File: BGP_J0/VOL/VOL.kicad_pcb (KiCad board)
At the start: 2 copper layers, 28 x 25 mm, 28 parts, among them J1 Conn_01x03_Female, P1 CONN_01X03, P2 CONN_01X02, P3 CONN_01X04, P4 CONN_01X02, P5 CONN_01X03, Q1 MMBF5457, Q2 MMBF5457

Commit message: Revert some changes
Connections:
- RV2 pad 1: /OUT -> Net-(RV2-Pad1)
- RV2 pad 3: Net-(RV2-Pad3) -> /I_BY
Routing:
- net /OUT: track 35.1 -> 28.5 mm
- net /I_BY: track 19.9 -> 24.2 mm

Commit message: Final J0 tone pot fixes
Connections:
- RV2 pad 1: Net-(RV2-Pad1) -> Net-(J1-Pad1)
- RV2 pad 2: Net-(J1-Pad1) -> /I_BY
- RV2 pad 3: /I_BY -> Net-(RV2-Pad3)
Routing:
- net Net-(J1-Pad1): track 10.4 -> 7.29 mm
- net /I_BY: track 24.2 -> 26.9 mm
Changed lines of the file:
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@@
   (general
     (links 49)
-    (no_connects 0)
+    (no_connects 3)
     (area 150.924999 70.924999 179.075001 96.075001)
     (thickness 1.6)
     (drawings 8)
-    (tracks 146)
+    (tracks 147)
     (zones 0)
     (modules 28)
@@
   (net 16 "Net-(J1-Pad2)")
   (net 17 "Net-(J1-Pad1)")
-  (net 18 "Net-(RV2-Pad1)")
+  (net 18 "Net-(RV2-Pad3)")
   (net_class Default "This is the default net class."
     (clearance 0.3)
@@
     (add_net "Net-(P1-Pad3)")
     (add_net "Net-(Q1-Pad2)")
-    (add_net "Net-(RV2-Pad1)")
+    (add_net "Net-(RV2-Pad3)")
   )
   (net_class PWR ""
@@
     (fp_line (start 2.1 10.7) (end -12.15 10.7) (layer B.CrtYd) (width 0.05))
     (pad 3 thru_hole circle (at 0 7.5 180) (size 1.8 1.8) (drill 1) (layers *.Cu *.Mask)
+      (net 18 "Net-(RV2-Pad3)"))
+    (pad 2 thru_hole circle (at 0 3.75 180) (size 1.8 1.8) (drill 1) (layers *.Cu *.Mask)
       (net 13 /I_BY))
-    (pad 2 thru_hole circle (at 0 3.75 180) (size 1.8 1.8) (drill 1) (layers *.Cu *.Mask)
+    (pad 1 thru_hole circle (at 0 0 180) (size 1.8 1.8) (drill 1) (layers *.Cu *.Mask)
       (net 17 "Net-(J1-Pad1)"))
-    (pad 1 thru_hole circle (at 0 0 180) (size 1.8 1.8) (drill 1) (layers *.Cu *.Mask)
-      (net 18 "Net-(RV2-Pad1)"))
     (pad 6 thru_hole circle (at -5 7.5 180) (size 1.8 1.8) (drill 1) (layers *.Cu *.Mask)
       (net 13 /I_BY))
@@
   (segment (start 162.8 88.1) (end 162.8 87.95) (width 0.3) (layer F.Cu) (net 12))
   (segment (start 163.8 73.3) (end 163.8 73.55) (width 0.3) (layer B.Cu) (net 12))
-  (segment (start 155.2 79.8) (end 155.25 79.85) (width 0.5) (layer F.Cu) (net 13))
-  (segment (start 155.2 73.3) (end 155.2 79.8) (width 0.5) (layer F.Cu) (net 13))
-  (segment (start 158 79.85) (end 155.25 79.85) (width 0.5) (layer F.Cu) (net 13))
+  (segment (start 158 79.85) (end 154.25 83.6) (width 0.5) (layer F.Cu) (net 13))
+  (segment (start 154.25 83.6) (end 153 83.6) (width 0.5) (layer F.Cu) (net 13))
+  (segment (start 155.2 73.3) (end 155.2 77.05) (width 0.5) (layer F.Cu) (net 13))
+  (segment (start 155.2 77.05) (end 158 79.85) (width 0.5) (layer F.Cu) (net 13))
   (segment (start 155.2 73.3) (end 155.2 73.05) (width 0.5) (layer F.Cu) (net 13))
   (segment (start 155.2 73.05) (end 156.5 71.75) (width 0.5) (layer F.Cu) (net 13))
@@
   (segment (start 165.8 73.05) (end 165.8 73.3) (width 0.5) (layer F.Cu) (net 13))
   (segment (start 164.5 71.75) (end 165.8 73.05) (width 0.5) (layer F.Cu) (net 13))
-  (segment (start 155.25 79.85) (end 153 79.85) (width 0.5) (layer F.Cu) (net 13))
   (segment (start 165.8 73.3) (end 165.8 73.05) (width 0.5) (layer B.Cu) (net 13))
   (segment (start 155.2 73.05) (end 155.2 73.3) (width 0.5) (layer B.Cu) (net 13))
@@
   (segment (start 174.4 92.7) (end 173.10051 92.7) (width 0.3) (layer F.Cu) (net 15))
   (segment (start 173.10051 92.7) (end 171 92.7) (width 0.5) (layer F.Cu) (net 15))
-  (segment (start 153 83.6) (end 155.46 86.06) (width 0.4) (layer F.Cu) (net 17))
-  (segment (start 155.46 86.06) (end 155.46 92.95) (width 0.4) (layer F.Cu) (net 17))
+  (segment (start 153 87.35) (end 153 91.64) (width 0.5) (layer F.Cu) (net 17))
+  (segment (start 153 91.64) (end 154.31 92.95) (width 0.5) (layer F.Cu) (net 17))
+  (segment (start 154.31 92.95) (end 155.46 92.95) (width 0.5) (layer F.Cu) (net 17))
   (zone (net 4) (net_name Earth) (layer B.Cu) (hatch edge 0.508)
     (connect_pads (clearance 0.3))

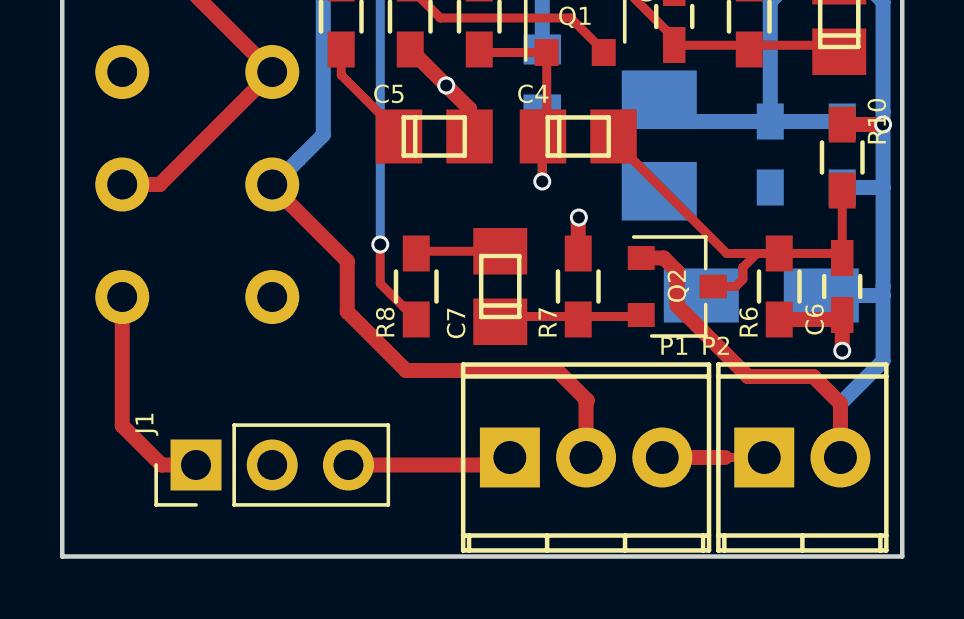
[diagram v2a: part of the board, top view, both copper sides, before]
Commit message: J0 VOL board modded for all CONN on bottom side
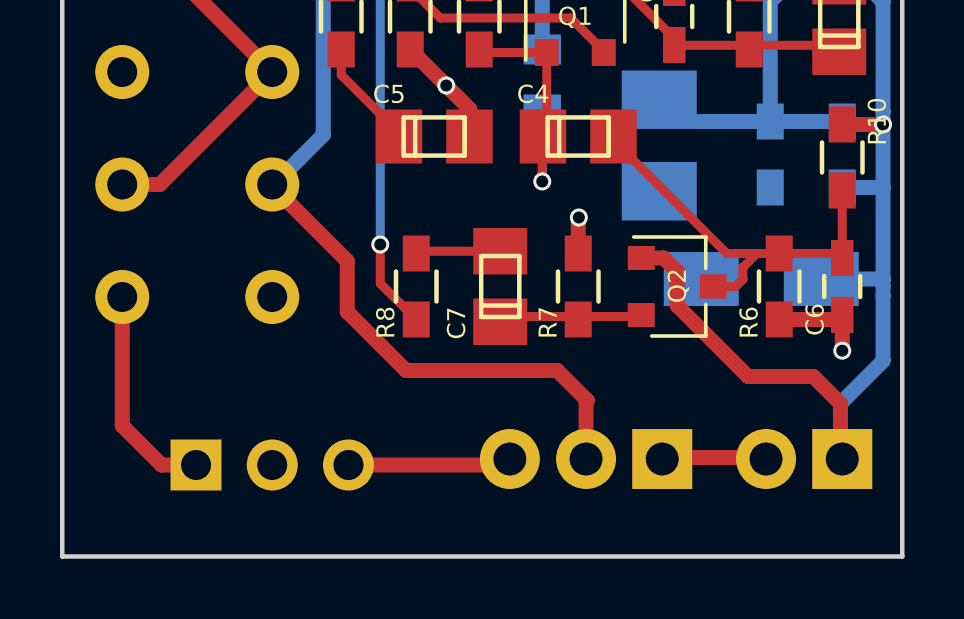
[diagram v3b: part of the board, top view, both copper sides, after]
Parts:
- J1, P1, P2: moved to B.Cu
- moved P1 5.08 mm to (171.0, 92.8), turned to 180 degrees
- moved P2 2.60 mm to (177.0, 92.8), turned to 180 degrees
- moved D1 0.55 mm to (174.3, 86.8)
- turned J1 to 270 degrees
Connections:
- P1 pad 1: Earth -> Net-(P1-Pad1)
- P1 pad 3: Net-(P1-Pad3) -> Earth
- P2 pad 1: Net-(P1-Pad3) -> VCC
- P2 pad 2: VCC -> Net-(P1-Pad1)
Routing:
- net Net-(P1-Pad3): track 3.40 -> 0.00 mm
- net Net-(P1-Pad1): track 0.00 -> 3.40 mm

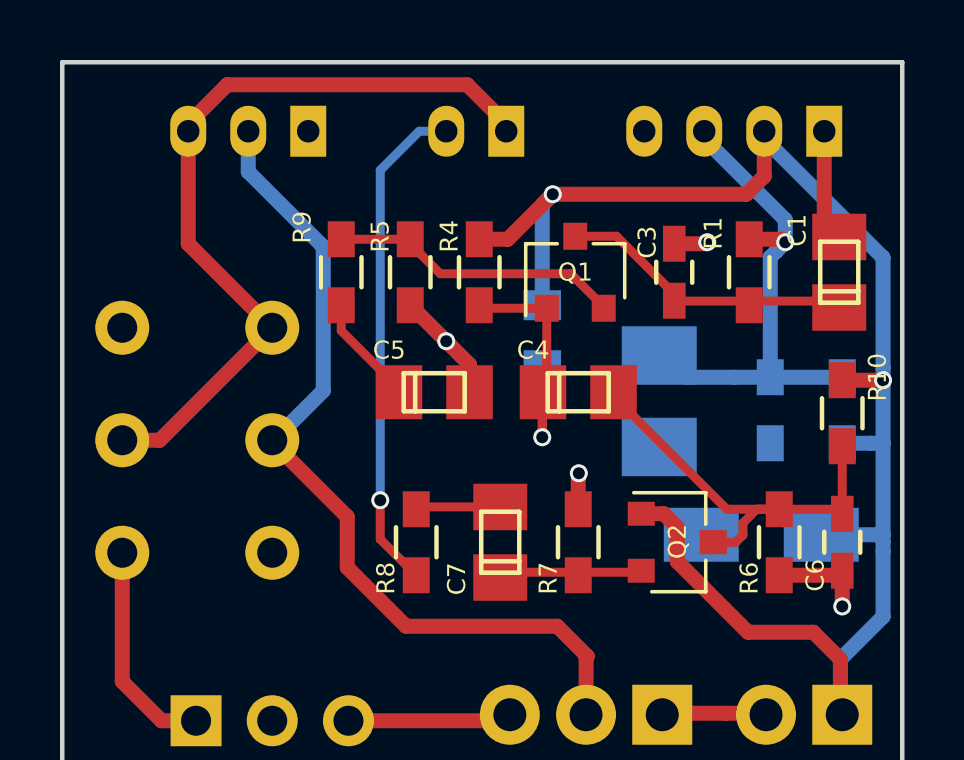
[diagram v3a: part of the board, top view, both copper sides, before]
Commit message: J0 VOL removed VOL CONN, slight rerouting
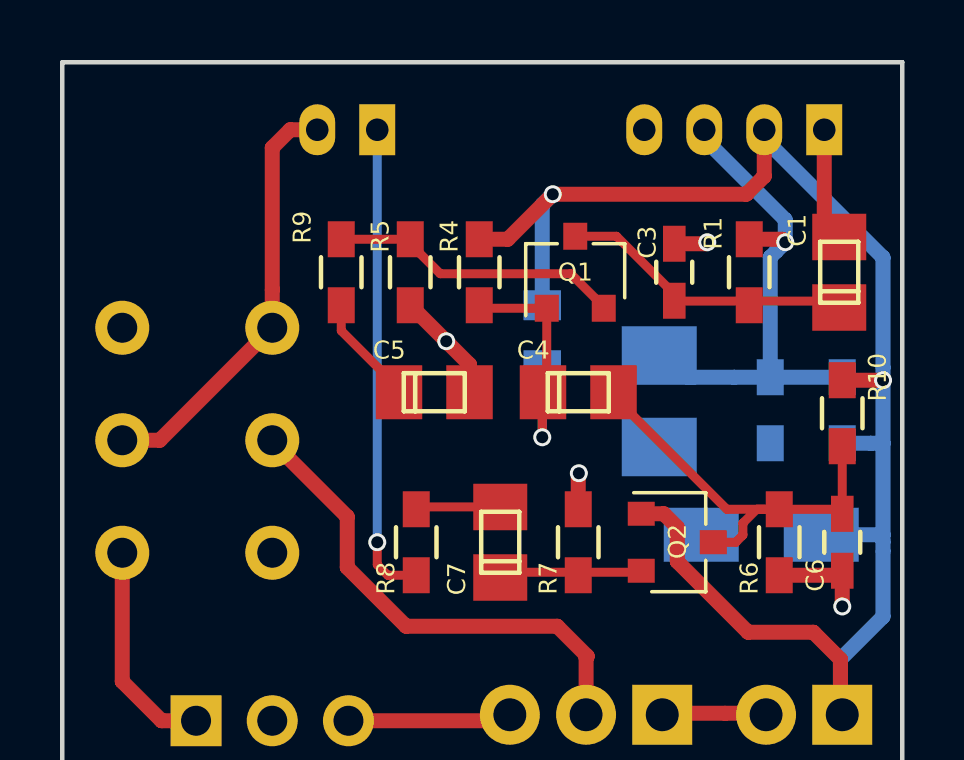
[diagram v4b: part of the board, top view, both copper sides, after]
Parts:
- removed P5: CONN_01X03, Connectors_JST:JST_PH_B3B-PH-K_03x2.00mm_Straight
- moved P4 4.30 mm to (161.5, 73.2)
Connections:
- P4 pad 1: /I_BY -> /O_BY
- P4 pad 2: /O_BY -> /I_BY
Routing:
- net /I_BY: track 26.9 -> 14.3 mm
- net /OUT: track 28.5 -> 16.4 mm
- net /O_BY: track 17.1 -> 16.1 mm

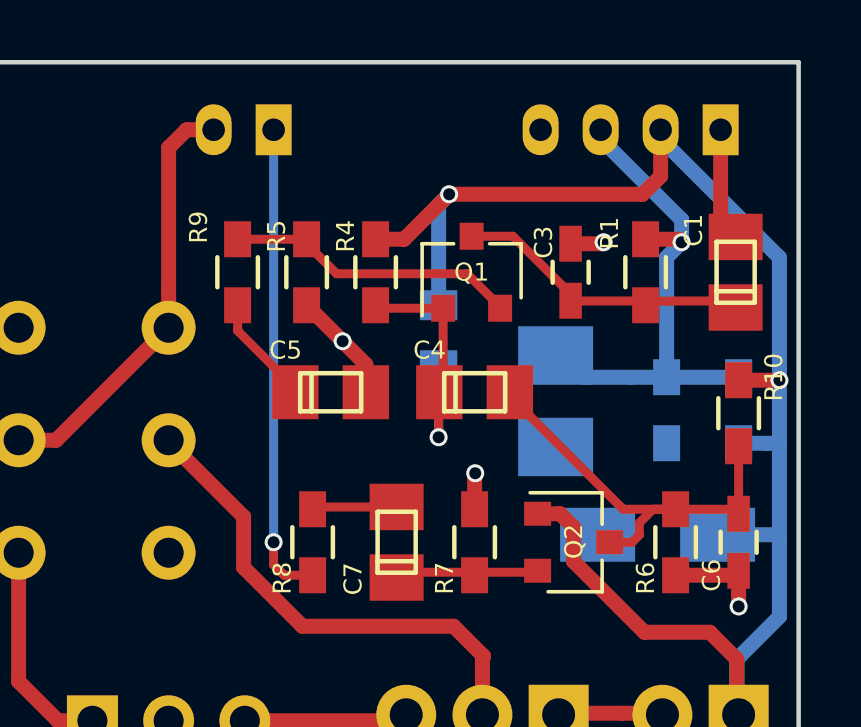
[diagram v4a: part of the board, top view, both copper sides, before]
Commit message: Normalising Schematics part list for J0
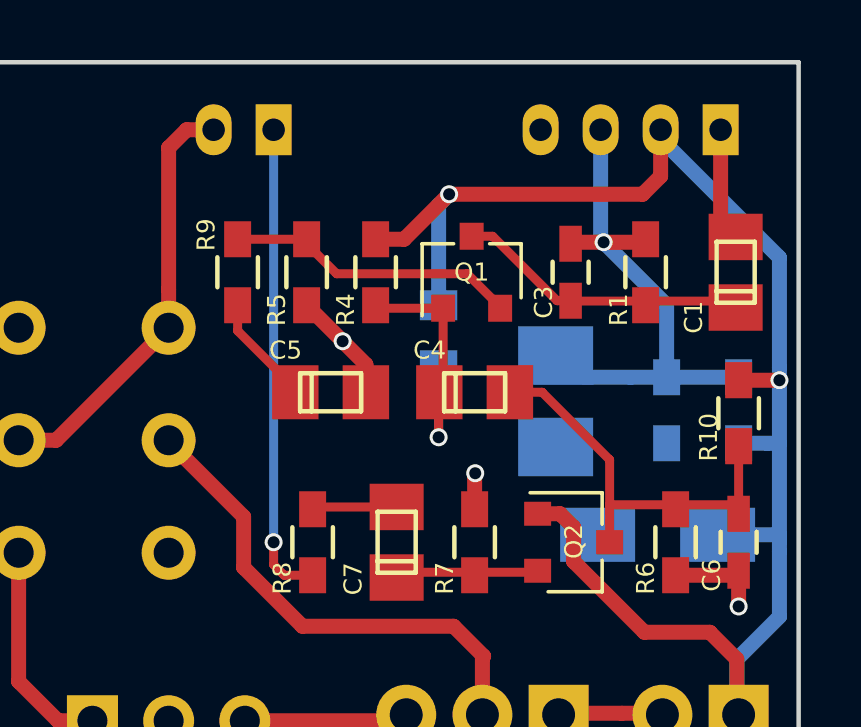
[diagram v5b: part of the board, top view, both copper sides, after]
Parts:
- R5: value 4.99k -> 3.9k
- R8: value 100 -> 10k
- R9: value 1.8k -> 1k
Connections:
- C3 pad 2: Earth -> /Vref
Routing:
- net /Vref: track 16.0 -> 17.3 mm
- net Earth: track 14.9 -> 13.8 mm, vias 4 -> 3
- net Net-(C4-Pad2): track 14.5 -> 13.8 mm

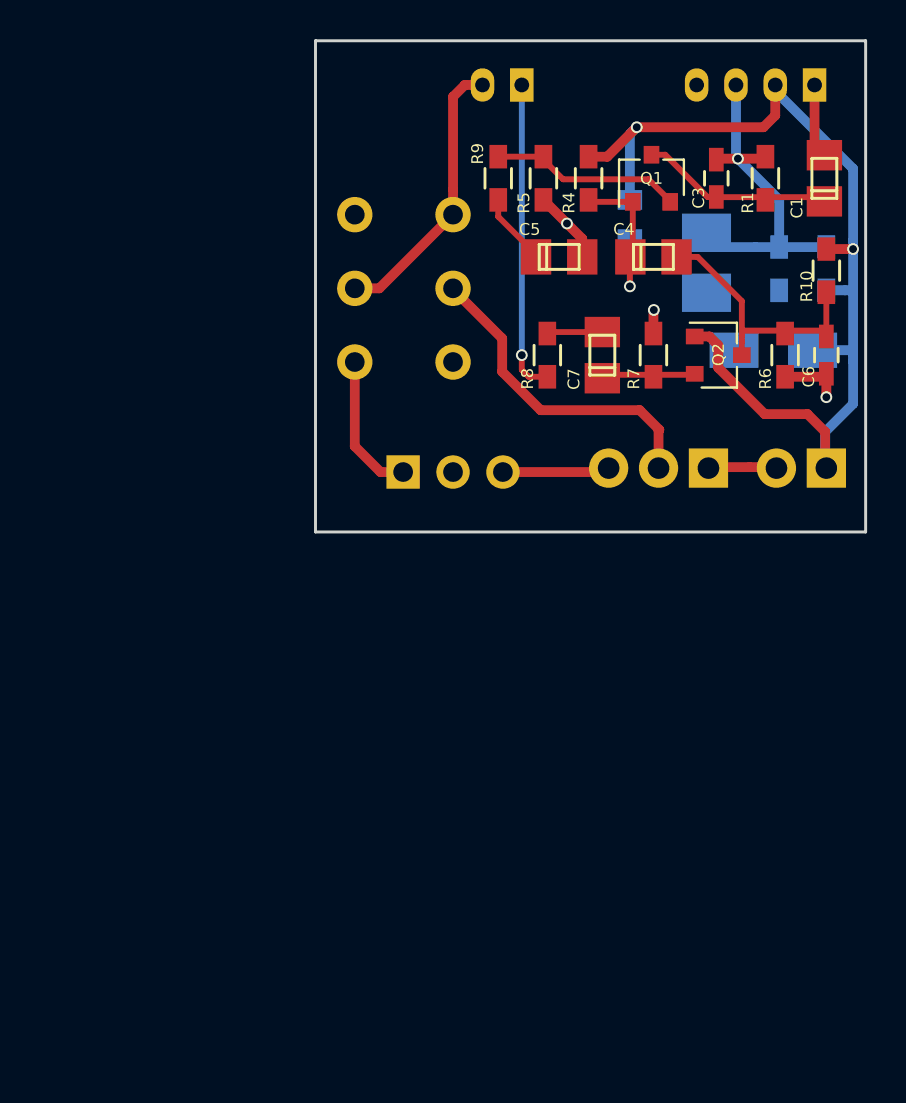
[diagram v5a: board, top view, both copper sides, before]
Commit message: J0 prepped for board run with blend board
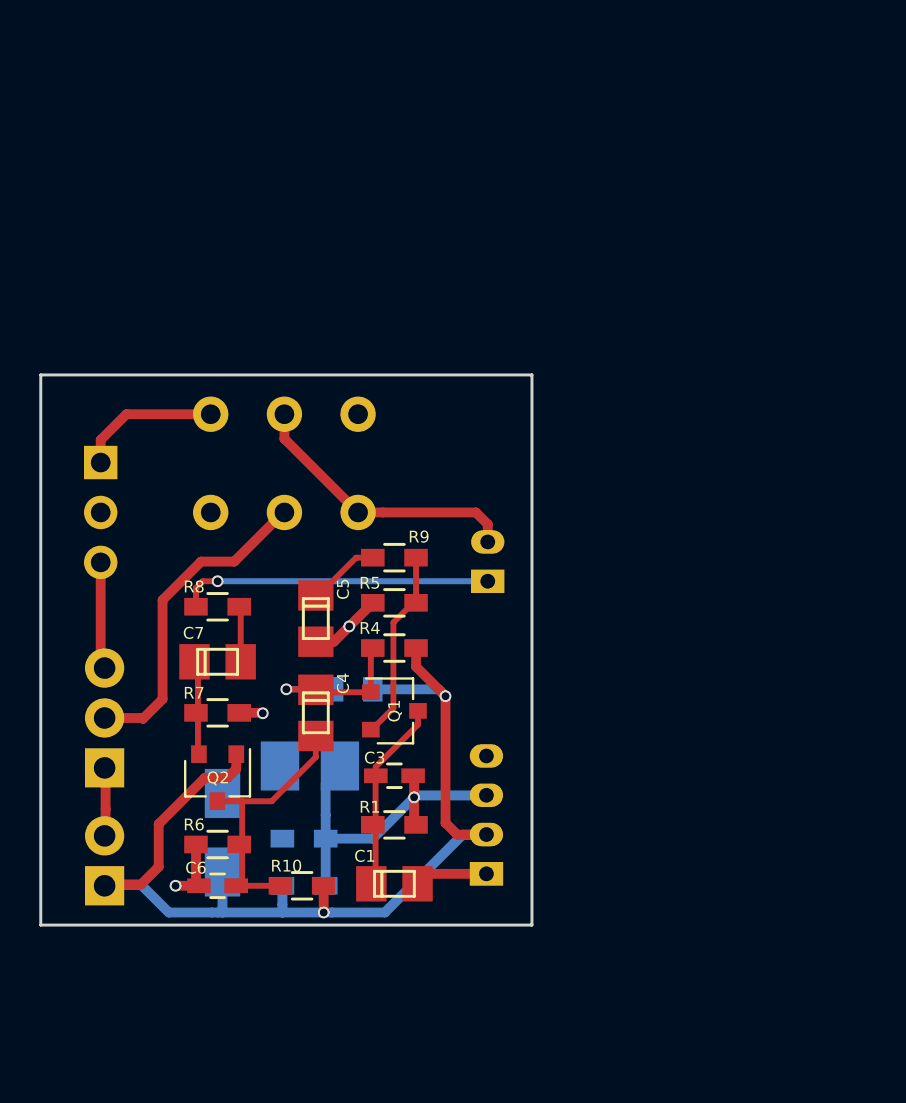
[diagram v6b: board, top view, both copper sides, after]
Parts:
- moved P3 43.5 mm to (159.7, 113.4), turned to 90 degrees
- moved P2 42.4 mm to (140.3, 114.0), turned to 90 degrees
- moved C1 42.0 mm to (155.0, 113.9), turned to 180 degrees
- moved R2 41.1 mm to (150.4, 114.0), turned to 0 degrees
- moved R10 41.1 mm to (150.3, 114.0), turned to 180 degrees
- moved C6 41.1 mm to (146.0, 114.0), turned to 180 degrees
- moved R6 38.1 mm to (146.0, 111.9), turned to 180 degrees
- moved R1 37.9 mm to (155.0, 110.9), turned to 0 degrees
- moved R3 37.8 mm to (150.4, 111.6), turned to 180 degrees
- moved D1 37.3 mm to (146.3, 111.3), turned to 90 degrees
- moved C3 34.5 mm to (155.0, 108.4), turned to 0 degrees
- moved P1 34.3 mm to (140.3, 108.0), turned to 90 degrees
- moved Q2 33.3 mm to (146.0, 108.5), turned to 270 degrees
- moved C2 32.6 mm to (150.7, 107.9), turned to 0 degrees
- moved Q1 30.1 mm to (155.0, 105.1), turned to 0 degrees
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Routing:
- net /IN: track 3.73 -> 4.42 mm
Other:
- board size 28 x 25 mm -> 25 x 28 mm

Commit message: J0 - Panelisation
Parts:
- moved P2 32.2 mm to (172.0, 119.8), turned to 180 degrees
- moved J1 29.4 mm to (150.4, 120.0), turned to 270 degrees
- moved P1 28.3 mm to (166.0, 119.8), turned to 180 degrees
- moved C6 26.0 mm to (172.0, 114.0), turned to 270 degrees
- moved RV2 24.5 mm to (148.0, 114.4), turned to 180 degrees
- moved R6 24.0 mm to (169.9, 114.0), turned to 270 degrees
- moved D1 23.2 mm to (169.3, 113.8), turned to 180 degrees
- moved R10 22.1 mm to (172.0, 109.7), turned to 270 degrees
- moved R2 22.0 mm to (172.0, 109.6), turned to 90 degrees
- moved Q2 21.2 mm to (166.5, 114.0), turned to 0 degrees
- moved R7 19.3 mm to (163.2, 114.0), turned to 90 degrees
- moved R3 19.3 mm to (169.6, 109.6), turned to 270 degrees
- moved C1 19.1 mm to (171.9, 105.0), turned to 270 degrees
- moved C7 18.5 mm to (160.6, 114.0), turned to 270 degrees
- moved R8 18.4 mm to (157.8, 114.0), turned to 90 degrees
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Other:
- board size 25 x 28 mm -> 28 x 25 mm

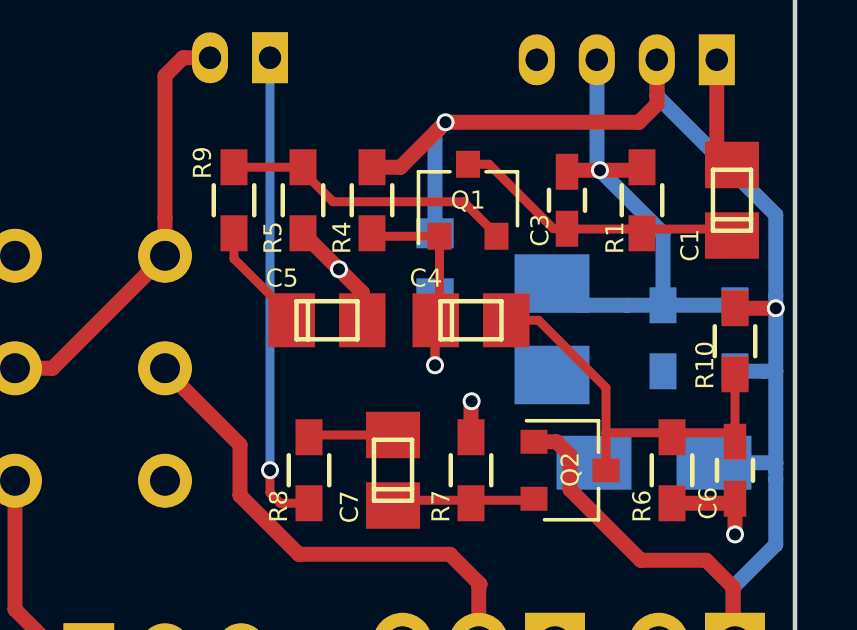
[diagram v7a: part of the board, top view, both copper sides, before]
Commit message: BOM complete and changes made to PCBs for cap changes
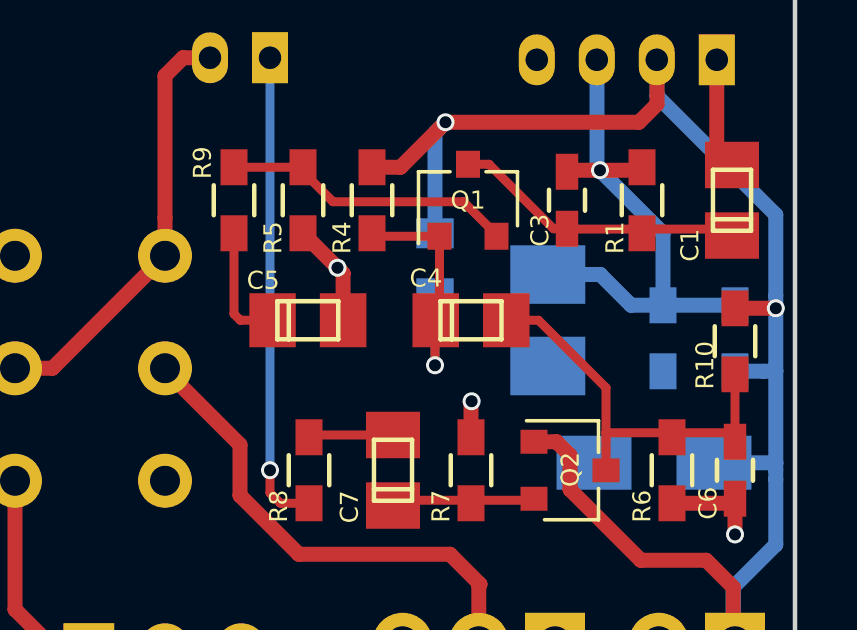
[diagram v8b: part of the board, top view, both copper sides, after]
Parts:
- C7: value 10u -> 1u
- moved C5 0.64 mm to (157.8, 109.0)
- moved C2 0.33 mm to (165.8, 109.0)
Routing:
- net /Vref: track 17.3 -> 18.8 mm
